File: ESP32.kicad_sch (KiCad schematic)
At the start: 25 parts, among them J1 USB_B_Micro, J2 BATT, J3 PMS7003 Connector, J4 BootSel, J5 UART, SW1 RESET, U1 ESP32-C3-MINI-1, U2 AMS1117-3.3, U3 AMS1117-5.0

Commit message: Rework of power + PCB cleanup
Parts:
- removed R3: 0, Resistor_SMD:R_0603_1608Metric_Pad0.98x0.95mm_HandSolder, symbol Device:R
- added D3, D4: SS14, Diode_SMD:D_SMA_Handsoldering, symbol Device:D_Schottky
- added Q1: AO3401A, Package_TO_SOT_SMD:SOT-23, symbol Transistor_FET:AO3401A
- J1: footprint Connector_USB:USB_Micro-B_Molex-105017-0001 -> Connector_USB:USB_Mini-B_Wuerth_65100516121_Horizontal
- J3: footprint Connector_PinSocket_1.00mm:PinSocket_2x05_P1.00mm_Vertical_SMD -> Connector_PinSocket_1.27mm:PinSocket_2x05_P1.27mm_Vertical_SMD
- R2: value 0 -> 10k
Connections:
- net GND: now also R2.2
- net VBUS: now also R2.1, D3.2 (A), Q1.1 (G)
- net 3v3_reg_vin: no longer names the net of C4.1, U2.3 (VI)
- net 3v3_reg_vin: now also D3.1 (K), D4.1 (K); no longer R2.2
- net 5v_reg_out: no longer names the net of C7.1, D2.2 (A), U3.2 (VO)
- net B+: no longer names the net of C6.1, U3.3 (VI)
- net B+: now also Q1.3 (D); no longer J2.2 (Pin_2), R2.1
- new net +BATT: D4.2 (A), J2.2 (Pin_2), Q1.2 (S)
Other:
- note added: "Este footprint no parece ser el correcto. Elegir uno explicito!"
- moved on the sheet: C4, C5, C6, C7, C8, D1, D2, R6, SW1, U2, U3

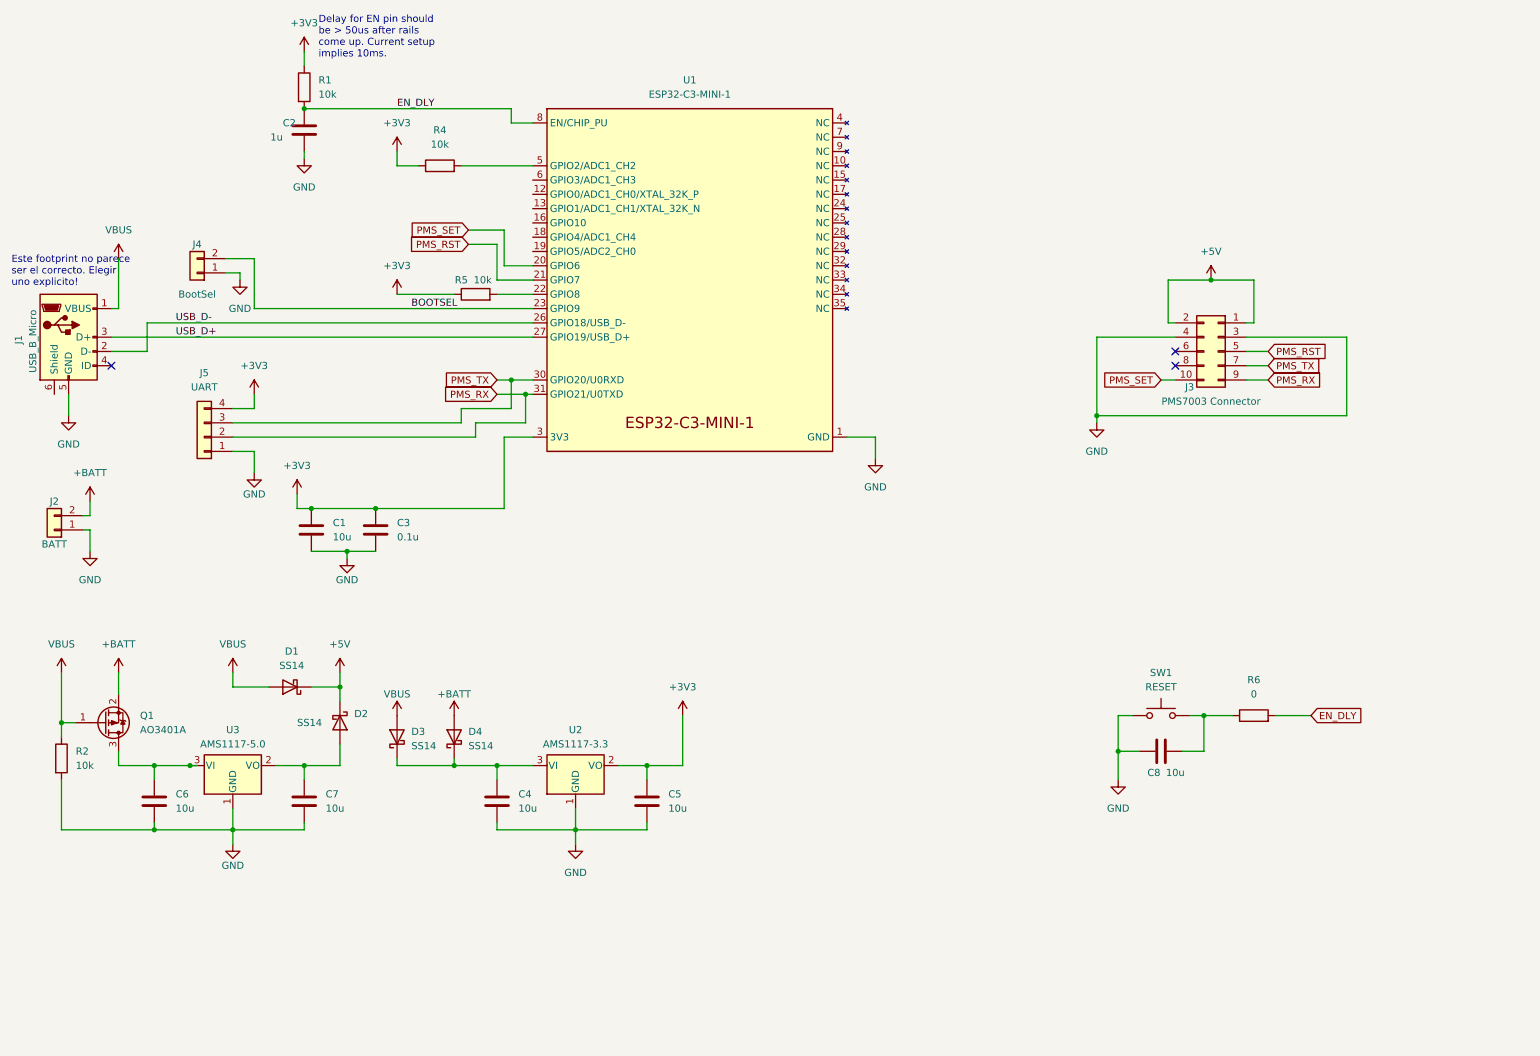
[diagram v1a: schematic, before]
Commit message: New layout routing
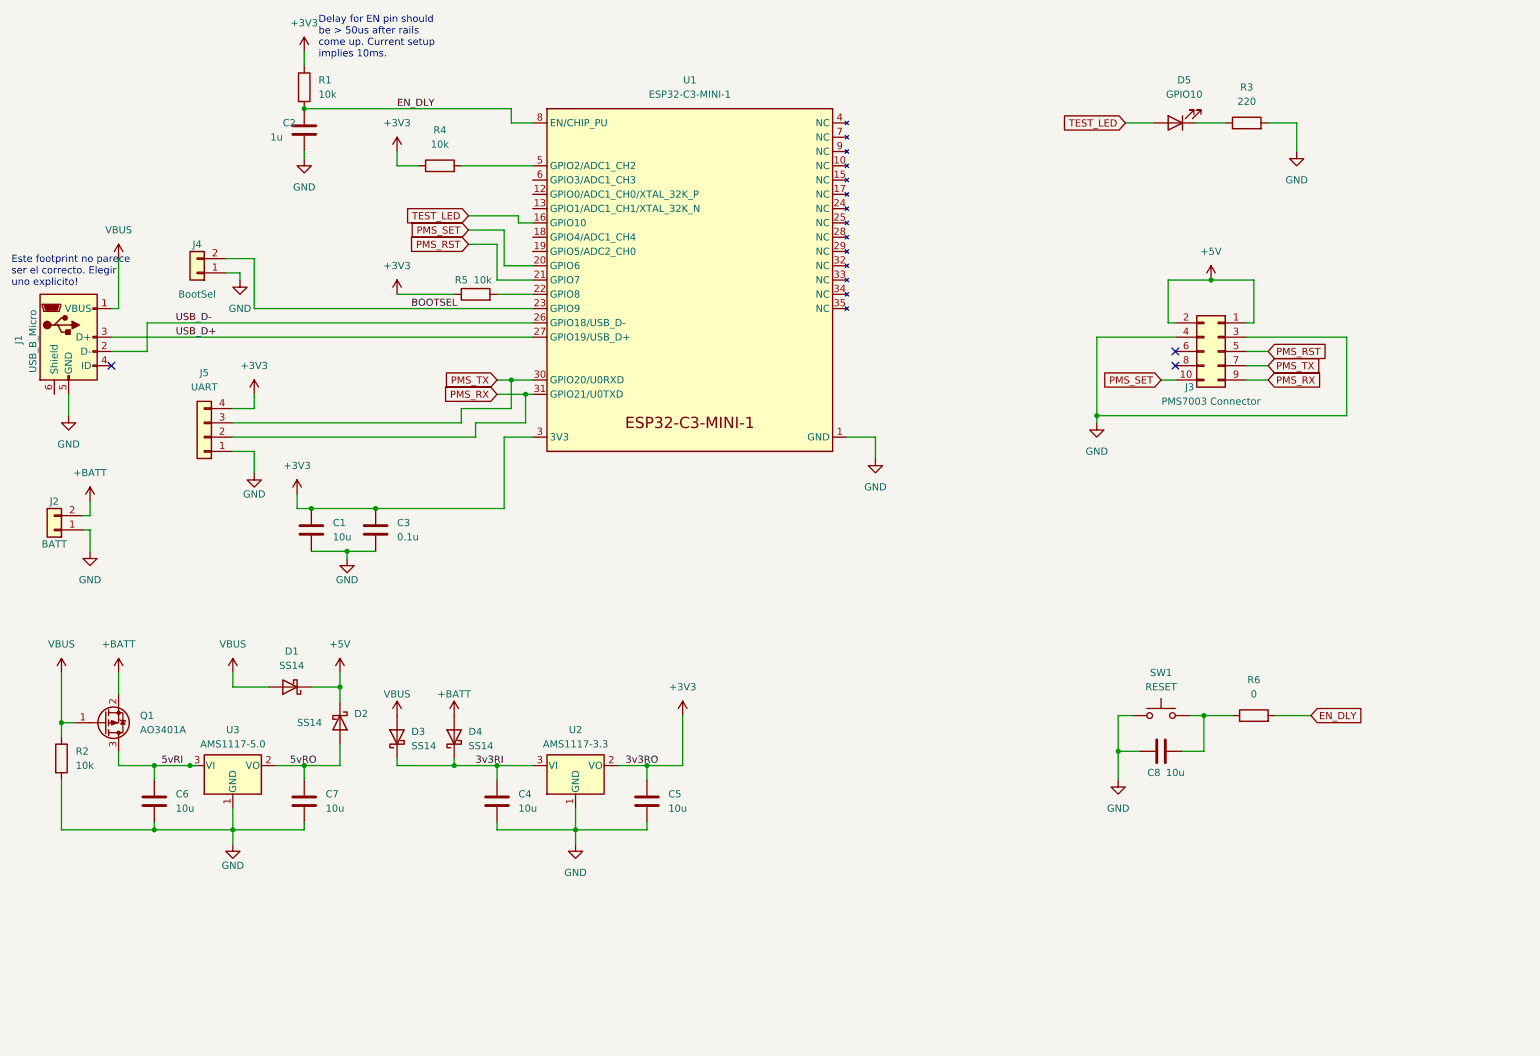
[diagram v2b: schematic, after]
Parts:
- added D5: GPIO10, LED_SMD:LED_0603_1608Metric_Pad1.05x0.95mm_HandSolder, symbol Device:LED
- added R3: 220, Resistor_SMD:R_0603_1608Metric_Pad0.98x0.95mm_HandSolder, symbol Device:R
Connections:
- net GND: now also R3.2
- net 5vRO: now reaches C7.1, D2.2 (A), U3.2 (VO)
- net 3v3RI: now reaches C4.1, D3.1 (K), D4.1 (K), U2.3 (VI)
- net TEST_LED: now reaches U1.16 (GPIO10)
- net TEST_LED: now also D5.2 (A)
- net 5vRI: now reaches C6.1, Q1.3 (D), U3.3 (VI)
- new net: D5.1 (K), R3.1
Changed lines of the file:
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@@
+    (stroke (width 0) (type default) (color 0 0 0 0))
+  )
+  (wire (pts (xy 95.25 50.8) (xy 104.14 50.8))
     (stroke (width 0) (type default) (color 0 0 0 0))
   )
@@
     (stroke (width 0) (type default) (color 0 0 0 0))
   )
+  (wire (pts (xy 237.49 34.29) (xy 242.57 34.29))
+    (stroke (width 0) (type default) (color 0 0 0 0))
+  )
   (wire (pts (xy 101.6 53.34) (xy 101.6 59.69))
     (stroke (width 0) (type default) (color 0 0 0 0))
   )
+  (wire (pts (xy 104.14 50.8) (xy 104.14 52.07))
+    (stroke (width 0) (type default) (color 0 0 0 0))
+  )
   (wire (pts (xy 210.82 139.7) (xy 213.36 139.7))
     (stroke (width 0) (type default) (color 0 0 0 0))
@@
     (stroke (width 0) (type default) (color 0 0 0 0))
   )
+  (wire (pts (xy 104.14 52.07) (xy 106.68 52.07))
+    (stroke (width 0) (type default) (color 0 0 0 0))
+  )
   (wire (pts (xy 39.37 158.75) (xy 39.37 160.02))
     (stroke (width 0) (type default) (color 0 0 0 0))
@@
     (stroke (width 0) (type default) (color 0 0 0 0))
   )
+  (wire (pts (xy 242.57 34.29) (xy 242.57 39.37))
+    (stroke (width 0) (type default) (color 0 0 0 0))
+  )
   (wire (pts (xy 27.94 106.68) (xy 27.94 110.49))
     (stroke (width 0) (type default) (color 0 0 0 0))
@@
     (stroke (width 0) (type default) (color 0 0 0 0))
   )
+  (wire (pts (xy 224.79 34.29) (xy 229.87 34.29))
+    (stroke (width 0) (type default) (color 0 0 0 0))
+  )
   (wire (pts (xy 127 158.75) (xy 127 160.02))
     (stroke (width 0) (type default) (color 0 0 0 0))
@@
   )
   (wire (pts (xy 53.34 85.09) (xy 57.15 85.09))
+    (stroke (width 0) (type default) (color 0 0 0 0))
+  )
+  (wire (pts (xy 212.09 34.29) (xy 217.17 34.29))
     (stroke (width 0) (type default) (color 0 0 0 0))
   )
@@
     (effects (font (size 1.27 1.27)) (justify left bottom))
   )
+  (label "3v3RO" (at 123.19 148.59 0)
+    (effects (font (size 1.27 1.27)) (justify left bottom))
+  )
+  (label "5vRO" (at 63.5 148.59 0)
+    (effects (font (size 1.27 1.27)) (justify left bottom))
+  )
+  (label "5vRI" (at 40.64 148.59 0)
+    (effects (font (size 1.27 1.27)) (justify left bottom))
+  )
   (label "BOOTSEL" (at 85.09 67.31 0)
+    (effects (font (size 1.27 1.27)) (justify left bottom))
+  )
+  (label "3v3RI" (at 96.52 148.59 0)
     (effects (font (size 1.27 1.27)) (justify left bottom))
   )
@@
     (effects (font (size 1.27 1.27)) (justify right))
     (property "Intersheet References" "${INTERSHEET_REFS}" (id 0) (at 84.6121 53.2606 0)
+      (effects (font (size 1.27 1.27)) (justify right) hide)
+    )
+  )
+  (global_label "TEST_LED" (shape input) (at 95.25 50.8 180) (fields_autoplaced)
+    (effects (font (size 1.27 1.27)) (justify right))
+    (property "Intersheet References" "${INTERSHEET_REFS}" (id 0) (at 84.1283 50.7206 0)
+      (effects (font (size 1.27 1.27)) (justify right) hide)
+    )
+  )
+  (global_label "TEST_LED" (shape input) (at 212.09 34.29 180) (fields_autoplaced)
+    (effects (font (size 1.27 1.27)) (justify right))
+    (property "Intersheet References" "${INTERSHEET_REFS}" (id 0) (at 200.9683 34.2106 0)
       (effects (font (size 1.27 1.27)) (justify right) hide)
     )
@@
     (pin "3")
   )
+  (symbol (lib_id "Device:R") (at 233.68 34.29 90) (unit 1)
+    (in_bom yes) (on_board yes) (fields_autoplaced)
+    (property "Reference" "R3" (id 0) (at 233.68 27.94 90))
+    (property "Value" "220" (id 1) (at 233.68 30.48 90))
+    (property "Footprint" "Resistor_SMD:R_0603_1608Metric_Pad0.98x0.95mm_HandSolder" (id 2) (at 233.68 36.068 90)
+      (effects (font (size 1.27 1.27)) hide)
+    )
+    (property "Datasheet" "~" (id 3) (at 233.68 34.29 0)
+      (effects (font (size 1.27 1.27)) hide)
+    )
+    (pin "1")
+    (pin "2")
+  )
   (symbol (lib_id "power:VBUS") (at 53.34 132.08 0) (unit 1)
     (in_bom yes) (on_board yes) (fields_autoplaced)
@@
     )
     (property "Datasheet" "" (id 3) (at 66.04 40.64 0)
+      (effects (font (size 1.27 1.27)) hide)
+    )
+    (pin "1")
+  )
+  (symbol (lib_id "Device:LED") (at 220.98 34.29 180) (unit 1)
+    (in_bom yes) (on_board yes) (fields_autoplaced)
+    (property "Reference" "D5" (id 0) (at 222.5675 26.67 0))
+    (property "Value" "GPIO10" (id 1) (at 222.5675 29.21 0))
+    (property "Footprint" "LED_SMD:LED_0603_1608Metric_Pad1.05x0.95mm_HandSolder" (id 2) (at 220.98 34.29 0)
+      (effects (font (size 1.27 1.27)) hide)
+    )
+    (property "Datasheet" "~" (id 3) (at 220.98 34.29 0)
+      (effects (font (size 1.27 1.27)) hide)
+    )
+    (pin "1")
+    (pin "2")
+  )
+  (symbol (lib_id "power:GND") (at 242.57 39.37 0) (unit 1)
+    (in_bom yes) (on_board yes) (fields_autoplaced)
+    (property "Reference" "#PWR0120" (id 0) (at 242.57 45.72 0)
+      (effects (font (size 1.27 1.27)) hide)
+    )
+    (property "Value" "GND" (id 1) (at 242.57 44.45 0))
+    (property "Footprint" "" (id 2) (at 242.57 39.37 0)
+      (effects (font (size 1.27 1.27)) hide)
+    )
+    (property "Datasheet" "" (id 3) (at 242.57 39.37 0)
       (effects (font (size 1.27 1.27)) hide)
     )
@@
       (reference "#PWR0119") (unit 1) (value "VBUS") (footprint "")
     )
+    (path "/ddc385e4-d488-44a2-86e6-1ca454908fd4"
+      (reference "#PWR0120") (unit 1) (value "GND") (footprint "")
+    )
     (path "/e13877fa-ddb4-491e-a148-095592913d6c"
       (reference "C1") (unit 1) (value "10u") (footprint "Capacitor_SMD:C_0603_1608Metric_Pad1.08x0.95mm_HandSolder")
@@
       (reference "D4") (unit 1) (value "SS14") (footprint "Diode_SMD:D_SMA_Handsoldering")
     )
+    (path "/d9eab112-5bdb-47b9-b033-2b78a5c8ec08"
+      (reference "D5") (unit 1) (value "GPIO10") (footprint "LED_SMD:LED_0603_1608Metric_Pad1.05x0.95mm_HandSolder")
+    )
     (path "/1f7e153c-4390-4c15-ace4-866a203e5e04"
       (reference "J1") (unit 1) (value "USB_B_Micro") (footprint "Connector_USB:USB_Mini-B_Wuerth_65100516121_Horizontal")
@@
       (reference "R2") (unit 1) (value "10k") (footprint "Resistor_SMD:R_0603_1608Metric_Pad0.98x0.95mm_HandSolder")
     )
+    (path "/b89b1a6b-b0a9-4388-8a90-8e6df4e39c24"
+      (reference "R3") (unit 1) (value "220") (footprint "Resistor_SMD:R_0603_1608Metric_Pad0.98x0.95mm_HandSolder")
+    )
     (path "/39d749f9-bee7-4d44-8420-5f14c9a7fc1c"

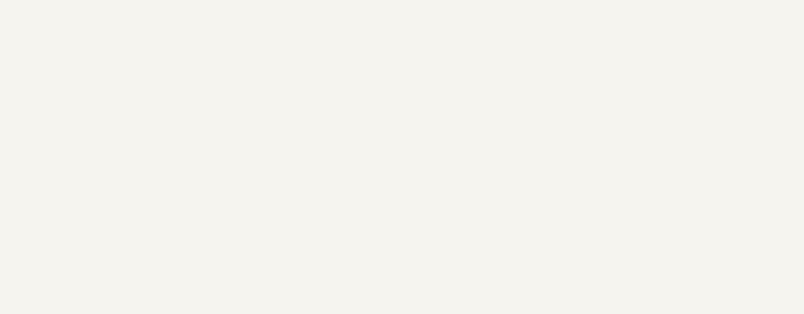
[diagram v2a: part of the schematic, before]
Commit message: Better power handling
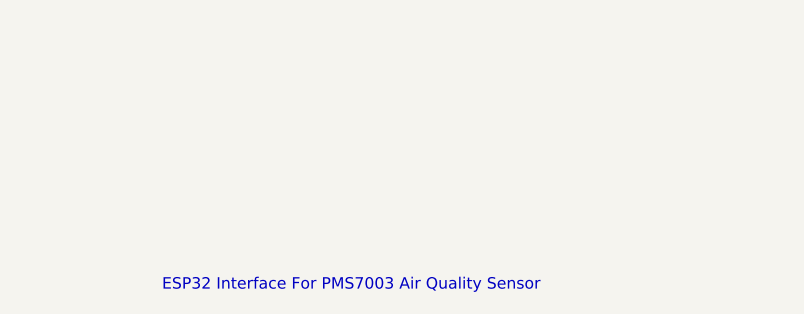
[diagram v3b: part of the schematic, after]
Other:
- note added: "ESP32 Interface For PMS7003 Air Quality Sensor"

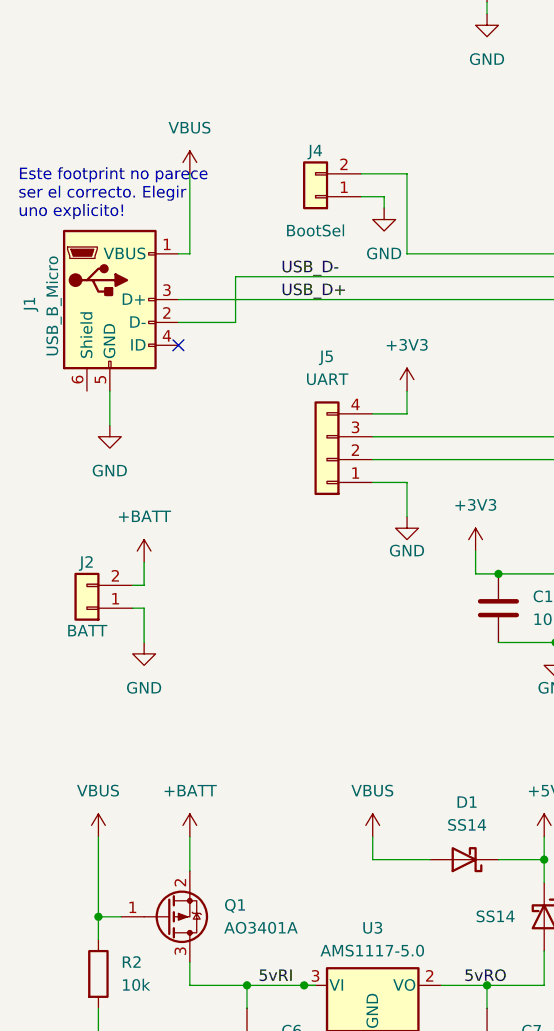
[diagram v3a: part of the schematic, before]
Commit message: Correct placement of the PMS header
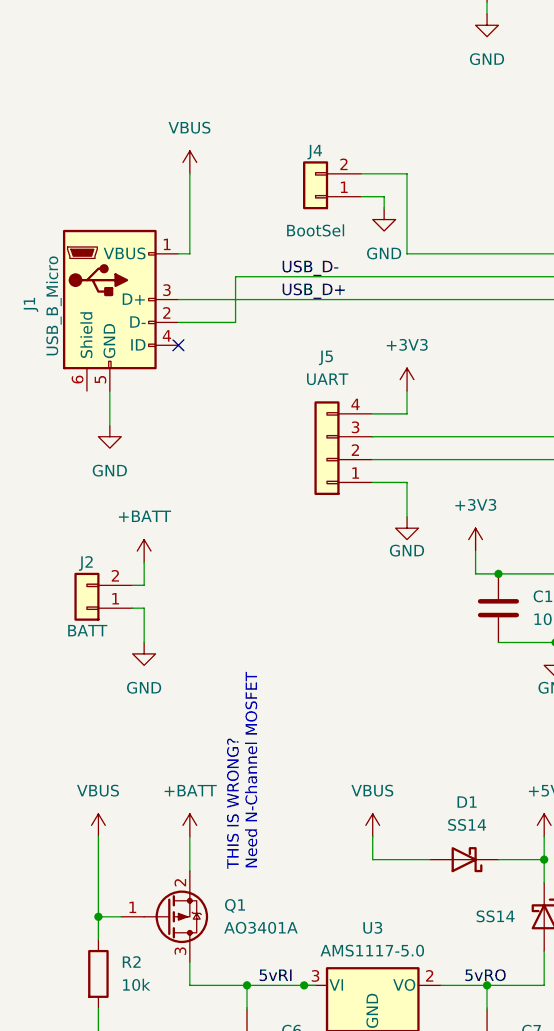
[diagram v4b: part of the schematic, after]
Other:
- note added: "THIS IS WRONG? Need N-Channel MOSFET"
- note removed: "Este footprint no parece ser el correcto. Elegir uno explicito!"
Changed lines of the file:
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@@
-    (effects (font (size 1.27 1.27)) (justify left bottom))
-  )
-  (text "Este footprint no parece\nser el correcto. Elegir\nuno explicito!"
-    (at 13.97 63.5 0)
     (effects (font (size 1.27 1.27)) (justify left bottom))
   )
@@
     (effects (font (size 1.27 1.27)) (justify left bottom))
   )
+  (text "THIS IS WRONG? \nNeed N-Channel MOSFET" (at 40.64 135.89 90)
+    (effects (font (size 1.27 1.27)) (justify left bottom))
+  )
